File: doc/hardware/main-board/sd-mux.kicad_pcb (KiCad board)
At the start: 2 copper layers, 50 x 132 mm, 54 parts, among them J1 SDCARD, P1 USB_OTG, P10 MKDS 1,5/3, P2 629105136821, P3 61400416021, P4 61400416021, P5 Conn_02x05_Odd_Even, P6 Conn_02x05_Odd_Even, P7 MKDS 1,5/3, Q1 IRF7606PBF, Q2 IRF7606PBF, Q3 IRF7606PBF, Q4 IRF7606PBF, Q5 2N7002, Q6 2N7002, Q7 IRF7606PBF, Q8 IRF7606PBF, U1 TS3USB30EDGSR, U2 FT245RL, U3 74AHC1G14, U4 TS3A27518E, U5 74AHC1G14

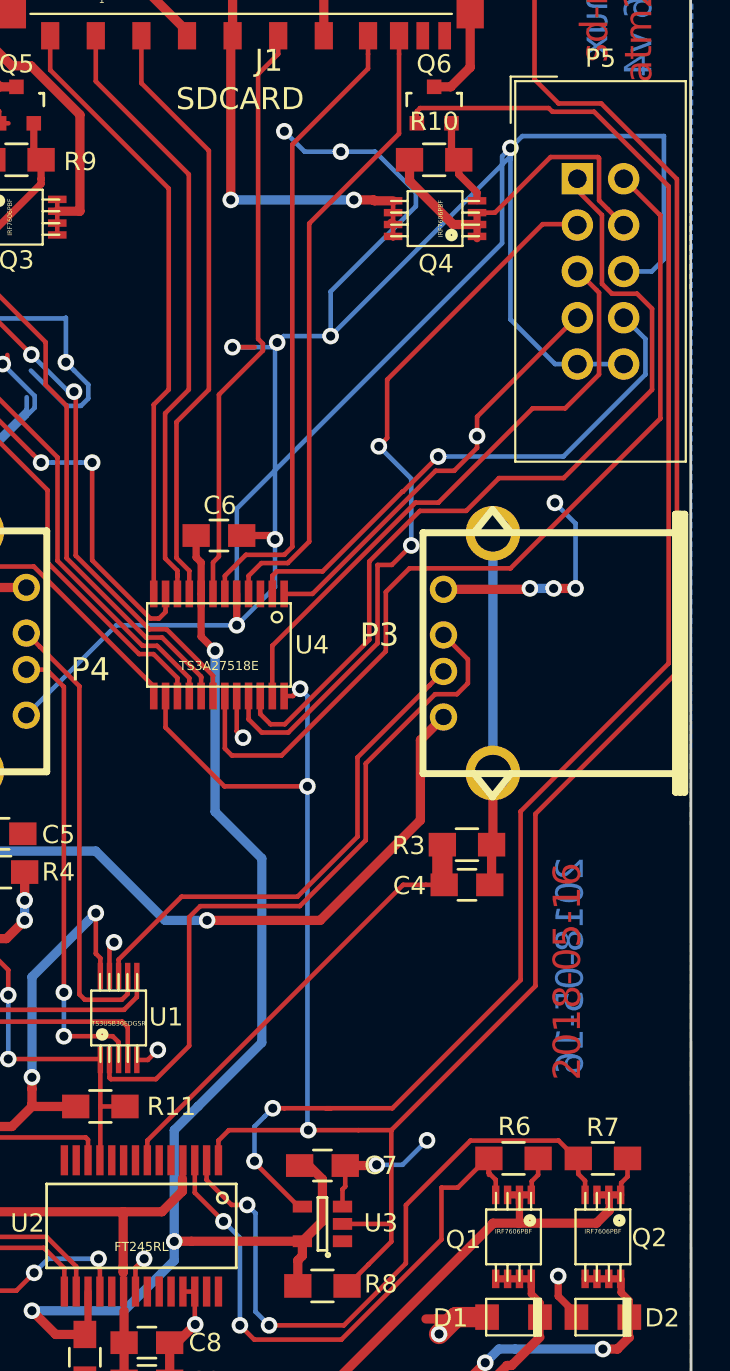
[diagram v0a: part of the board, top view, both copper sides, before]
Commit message: Pin out spare GPIOs to a header, eg to match ebay '4 channel relay module Arduino RPi'
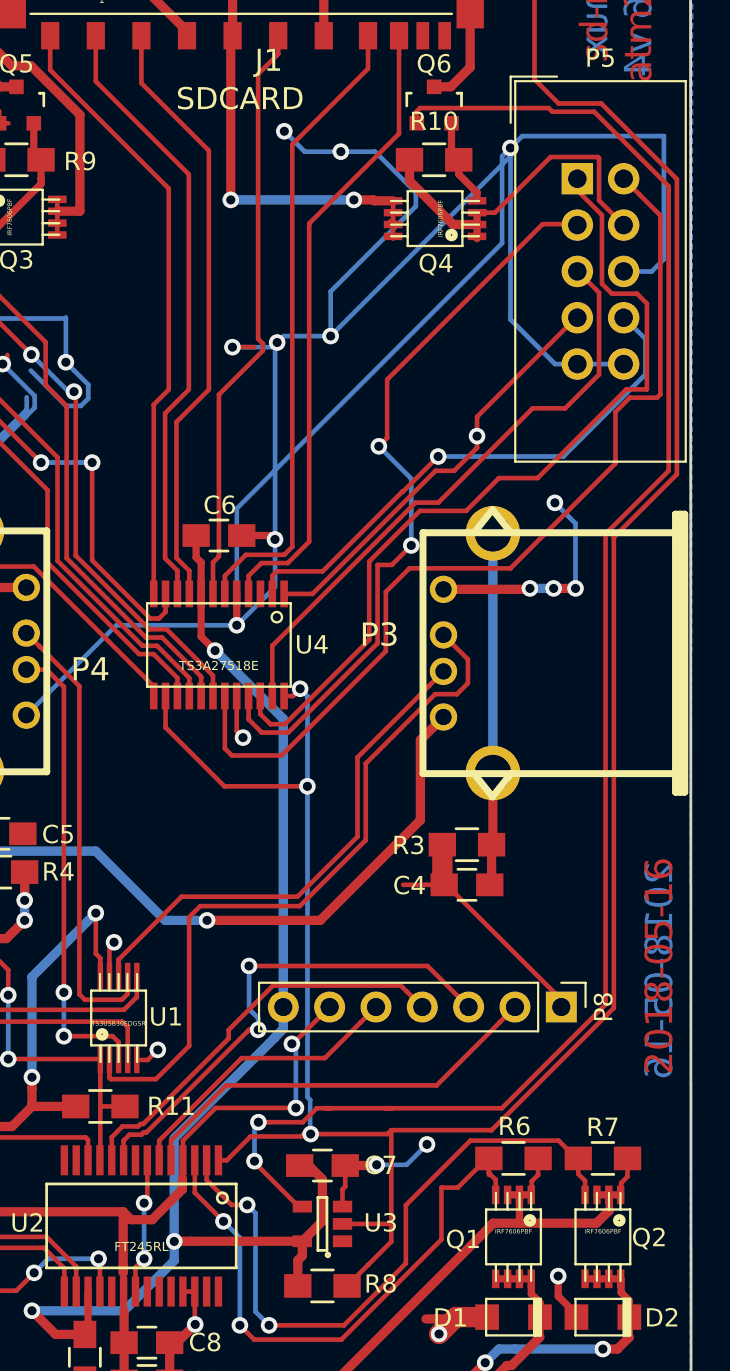
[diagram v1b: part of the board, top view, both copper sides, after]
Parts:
- added P8: CONN_01X07, Connector_PinHeader_2.54mm:PinHeader_1x07_P2.54mm_Vertical, F.Cu at (161.1, 86.9)
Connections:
- U2 pad 10: Net-(U2-Pad10) -> /GP2
- U2 pad 5: Net-(U2-Pad5) -> /GP0
- U2 pad 6: Net-(U2-Pad6) -> /GP3
- U2 pad 9: Net-(U2-Pad9) -> /GP1
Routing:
- net /GP1: track 0.00 -> 27.6 mm, vias 0 -> 2
- net /GP0: track 0.00 -> 23.0 mm
- net /GP2: track 0.00 -> 22.5 mm
- net /GP3: track 0.00 -> 16.0 mm
- net VDD: track 93.1 -> 107.9 mm, vias 2 -> 4
- net GND: track 340.3 -> 334.2 mm, vias 31 -> 32
- net Net-(Q6-Pad1): track 87.0 -> 90.9 mm
- net /SOCKET_SEL: track 184.1 -> 186.8 mm
- net +3V3: track 73.1 -> 74.0 mm
- net /DAT3_DUT: track 50.5 -> 51.3 mm

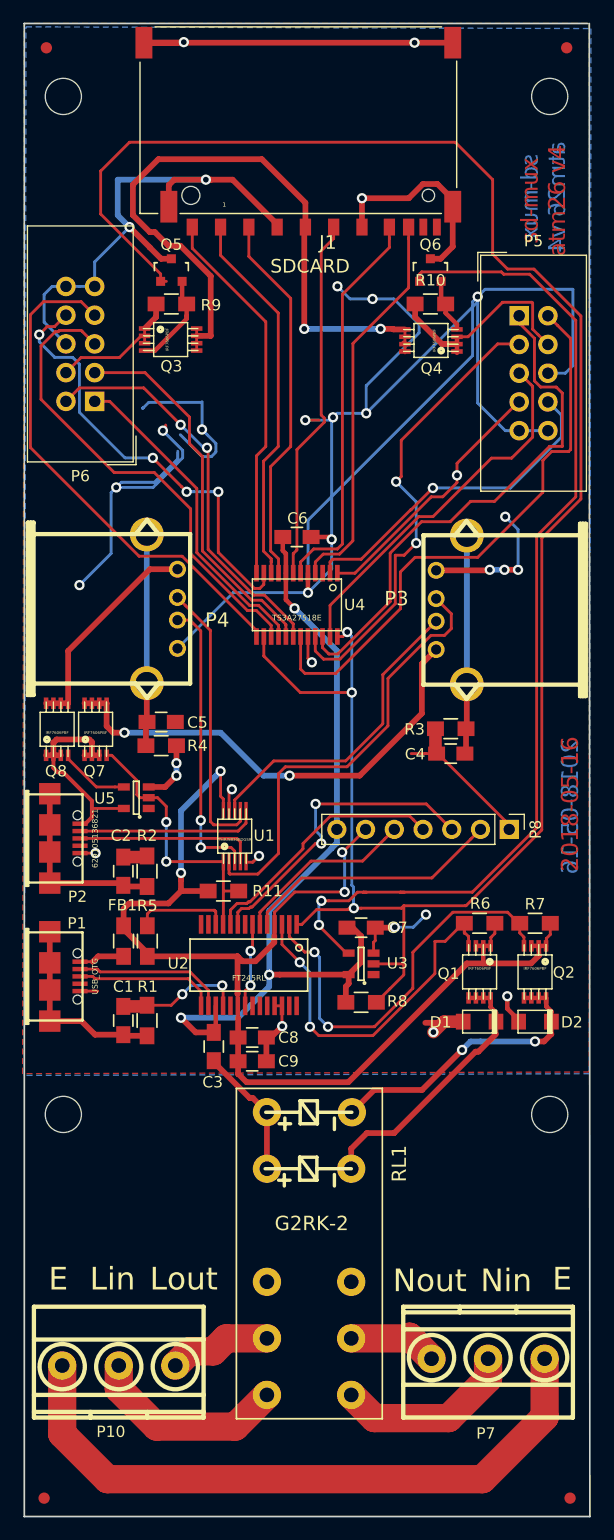
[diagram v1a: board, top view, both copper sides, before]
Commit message: Label up inputs and add URL in silk
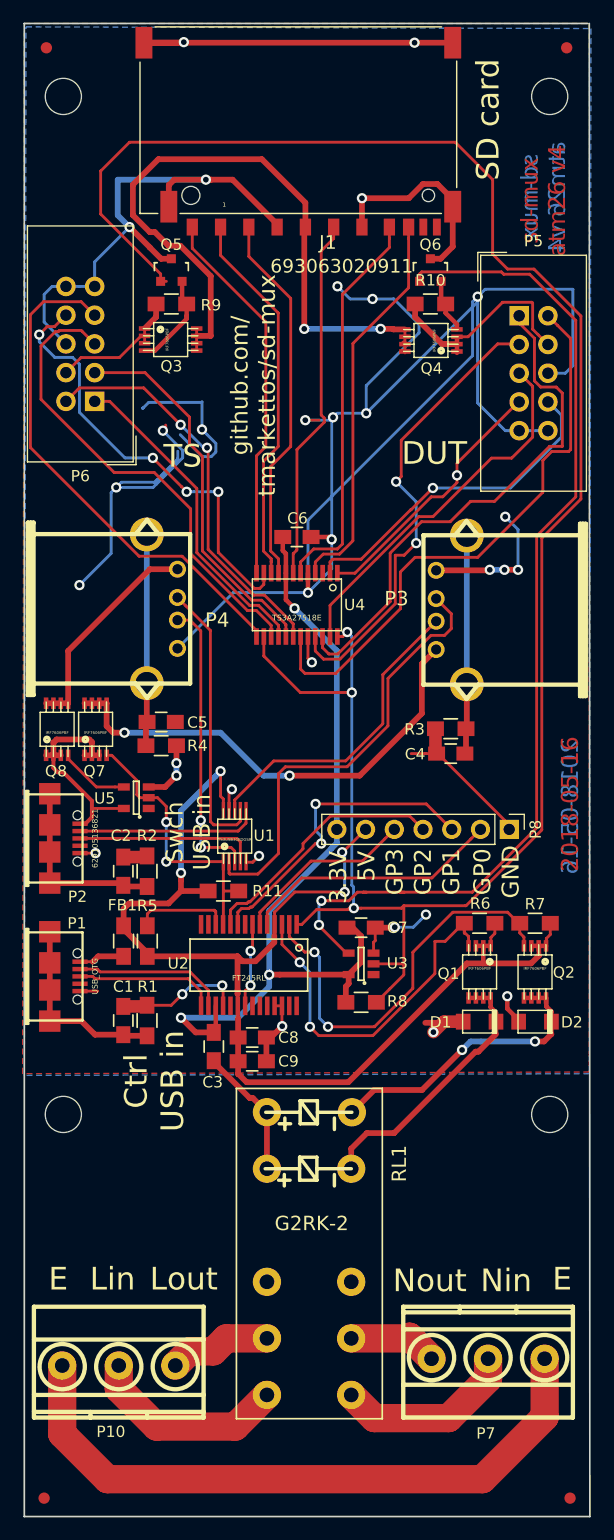
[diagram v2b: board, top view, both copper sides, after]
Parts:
- J1: value SDCARD -> 693063020911
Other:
- board text added: "3.3V"
- board text added: "5V"
- board text added: "Ctrl USB in"
- board text added: "DUT"
- board text added: "GND"
- board text added: "GP0"
- board text added: "GP1"
- board text added: "GP2"
- board text added: "GP3"
- board text added: "SD card"
- board text added: "Swch USB in"
- board text added: "TS"
- board text added: "github.com/ tmarkettos/sd-mux"
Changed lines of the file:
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@@
     (area 118.124519 15.525479 168.274521 147.675481)
     (thickness 1.6)
-    (drawings 19)
+    (drawings 32)
     (tracks 921)
     (zones 0)
@@
       (effects (font (size 1.2065 1.2065) (thickness 0.1016)) (justify left bottom))
     )
-    (fp_text value SDCARD (at 2.4826 -4.1704 180) (layer F.SilkS)
+    (fp_text value 693063020911 (at 2.4826 -4.1704 180) (layer F.SilkS)
       (effects (font (size 1.2065 1.2065) (thickness 0.1016)) (justify left bottom))
     )
@@
     )
   )
+  (gr_text "github.com/\ntmarkettos/sd-mux" (at 138.44952 47.60048 90) (layer F.SilkS)
+    (effects (font (size 1.5 1.5) (thickness 0.3)))
+  )
+  (gr_text 3.3V (at 145.94952 91.10048 90) (layer F.SilkS)
+    (effects (font (size 1.5 1.5) (thickness 0.3)))
+  )
+  (gr_text 5V (at 148.44952 90.10048 90) (layer F.SilkS)
+    (effects (font (size 1.5 1.5) (thickness 0.3)))
+  )
+  (gr_text GP3 (at 150.94952 90.60048 90) (layer F.SilkS)
+    (effects (font (size 1.5 1.5) (thickness 0.3)))
+  )
+  (gr_text GP2 (at 153.44952 90.60048 90) (layer F.SilkS)
+    (effects (font (size 1.5 1.5) (thickness 0.3)))
+  )
+  (gr_text GP1 (at 155.94952 90.60048 90) (layer F.SilkS)
+    (effects (font (size 1.5 1.5) (thickness 0.3)))
+  )
+  (gr_text GP0 (at 158.69952 90.60048 90) (layer F.SilkS)
+    (effects (font (size 1.5 1.5) (thickness 0.3)))
+  )
+  (gr_text GND (at 161.19952 90.60048 90) (layer F.SilkS)
+    (effects (font (size 1.5 1.5) (thickness 0.3)))
+  )
+  (gr_text "Swch\nUSB in" (at 132.69952 87.10048 90) (layer F.SilkS)
+    (effects (font (size 1.5 1.5) (thickness 0.3)))
+  )
+  (gr_text "Ctrl\nUSB in" (at 129.69952 109.10048 90) (layer F.SilkS)
+    (effects (font (size 2 2) (thickness 0.3)))
+  )
+  (gr_text "SD card" (at 159.19952 24.10048 90) (layer F.SilkS)
+    (effects (font (size 2 2) (thickness 0.3)))
+  )
+  (gr_text TS (at 132.19952 53.85048) (layer F.SilkS)
+    (effects (font (size 2 2) (thickness 0.3)))
+  )
+  (gr_text DUT (at 154.44952 53.60048) (layer F.SilkS)
+    (effects (font (size 2 2) (thickness 0.3)))
+  )
   (gr_text Nout (at 154.04952 126.75048) (layer F.SilkS)

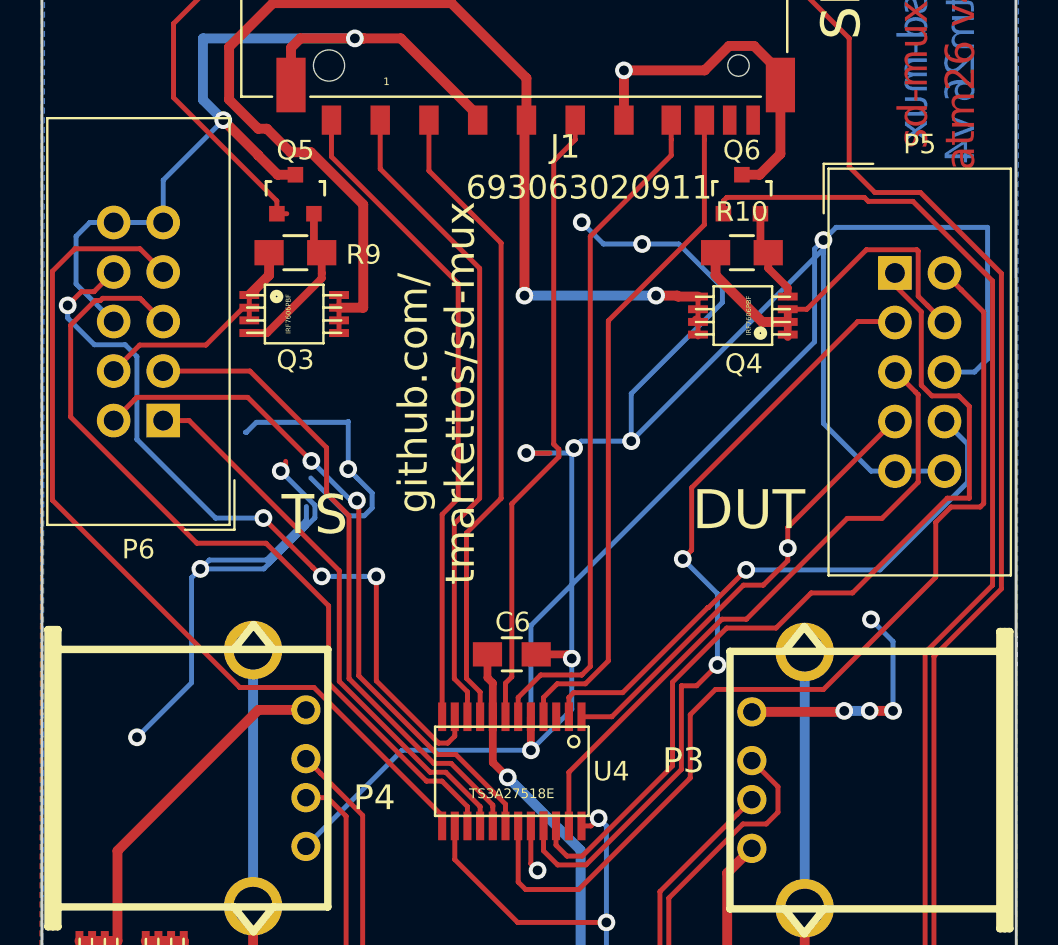
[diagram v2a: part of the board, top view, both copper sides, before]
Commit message: Move up IDC connector to be symmetrical
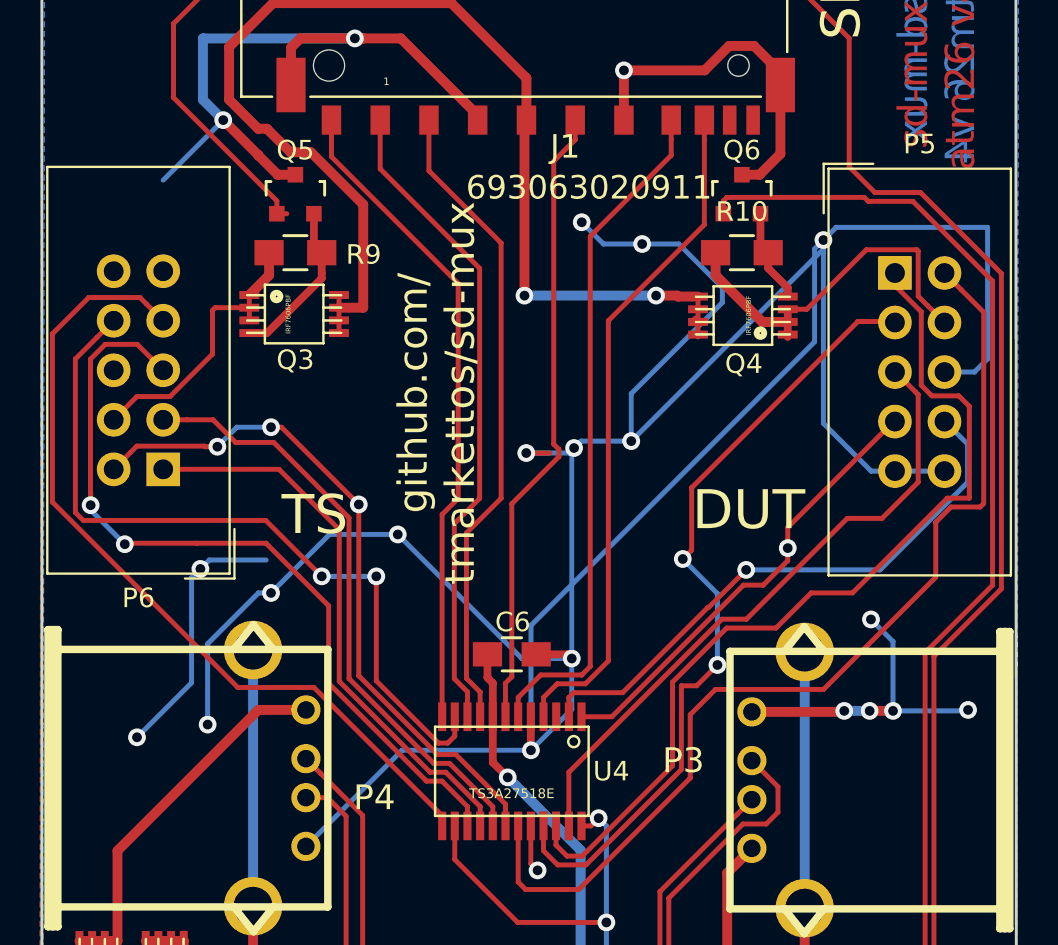
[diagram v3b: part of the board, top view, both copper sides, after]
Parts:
- moved P6 2.50 mm to (124.4, 51.5)
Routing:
- net (no net): track 45.4 -> 13.5 mm, vias 4 -> 2
- net GND: track 334.2 -> 353.7 mm, vias 32 -> 36
- net /DAT0_TS: track 46.3 -> 42.7 mm
- net /VDD_TS: track 12.2 -> 14.9 mm
- net /CMD_TS: track 33.5 -> 30.9 mm
- net /CLK_TS: track 42.0 -> 41.3 mm, vias 0 -> 2
- net /DAT1_TS: track 39.4 -> 39.3 mm, vias 4 -> 2
- net /DAT3_TS: vias 2 -> 3

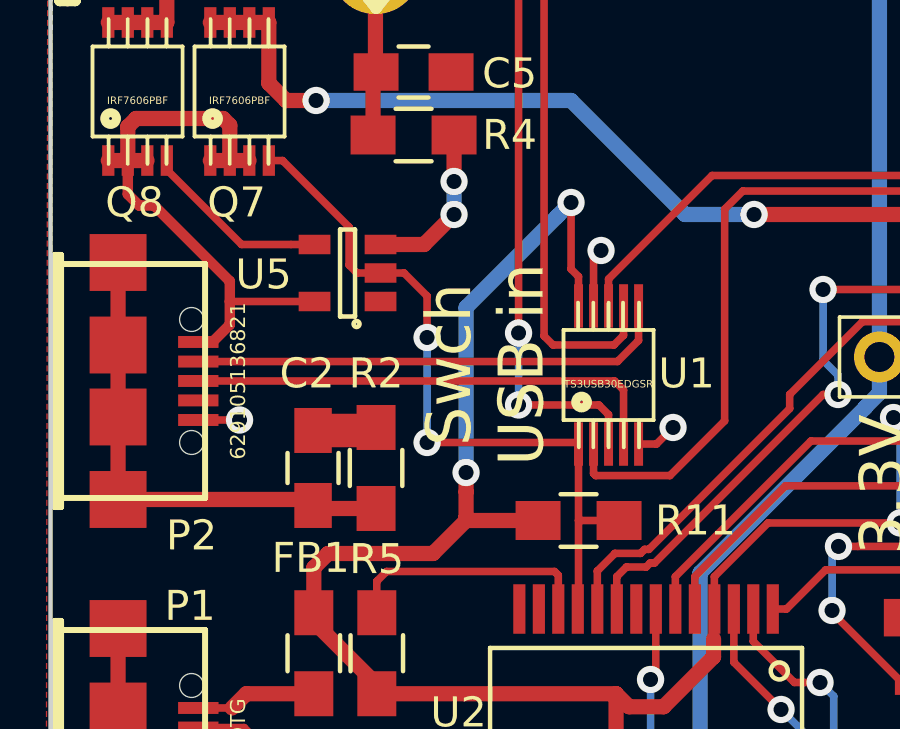
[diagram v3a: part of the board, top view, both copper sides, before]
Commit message: Remove origin mark that confuses DirtyPCBs
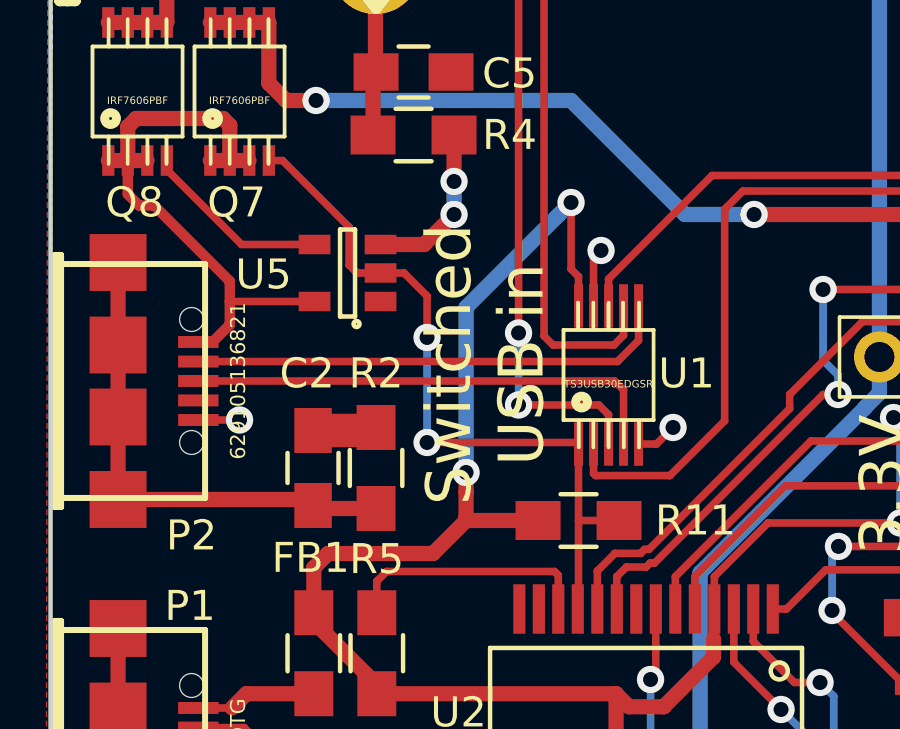
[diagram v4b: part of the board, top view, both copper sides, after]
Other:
- board text added: "Switched USB in"
- board text removed: "Swch USB in"
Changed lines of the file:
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@@
     (links 182)
     (no_connects 0)
-    (area 118.124519 15.525479 168.274521 147.675481)
+    (area 104.235236 14.97548 206.692858 187)
     (thickness 1.6)
-    (drawings 32)
+    (drawings 31)
     (tracks 904)
     (zones 0)
@@
       (drillshape 0)
       (scaleselection 1)
-      (outputdirectory ../fabrication/sd-mux-atm26-v3/))
+      (outputdirectory ../fabrication/sd-mux-atm26-v4/))
   )
   (net 0 "")
@@
     (effects (font (size 1.5 1.5) (thickness 0.3)))
   )
-  (gr_text "Swch\nUSB in" (at 132.69952 87.10048 90) (layer F.SilkS)
+  (gr_text "Switched\nUSB in" (at 132.69952 87.10048 90) (layer F.SilkS)
     (effects (font (size 1.5 1.5) (thickness 0.3)))
   )
@@
     (effects (font (size 1.5 1.5) (thickness 0.3)))
   )
-  (target plus (at 145.75 144.75) (size 5) (width 0.15) (layer Edge.Cuts))
   (gr_text "sd-mux\natm26 v4\n" (at 164.09952 30.95048 90) (layer B.Cu)
     (effects (font (size 1.5 1.5) (thickness 0.3)) (justify mirror))
